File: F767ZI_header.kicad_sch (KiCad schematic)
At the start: 21 parts, among them J2 CAN1, J3 CAN2, J4 UART, J5 PowerBoard, J6 EMERSW_CON, J7 I2C1_default, J9 RESET_SW, SW1 SW_Push, U1 MCP2562-E-P, U2 MCP2562-E-P

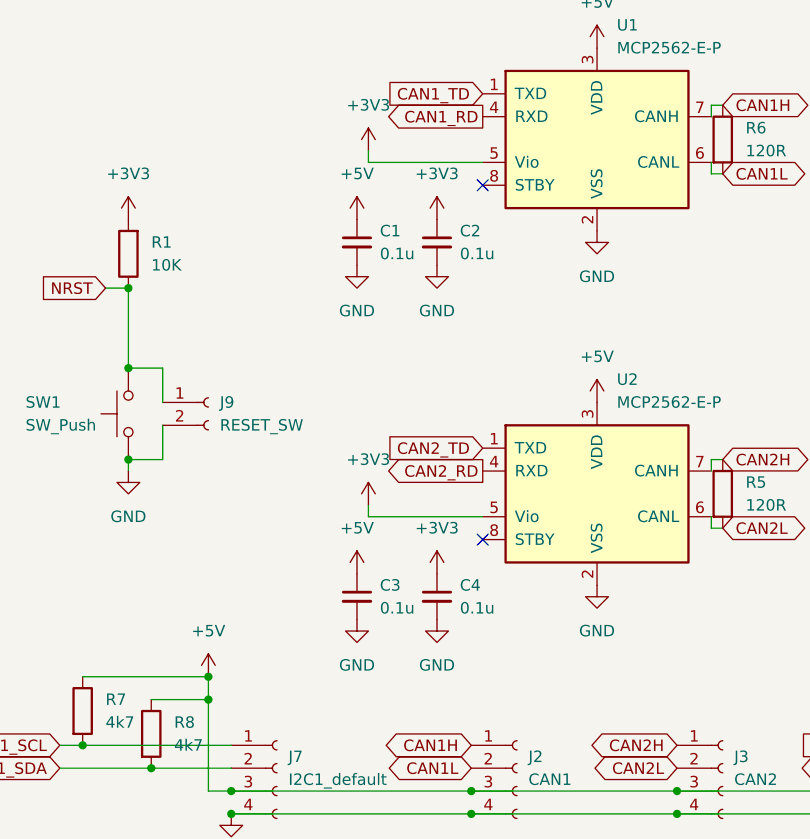
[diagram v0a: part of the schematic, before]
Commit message: SCH: トランシーバのSTBYをGNDに接続
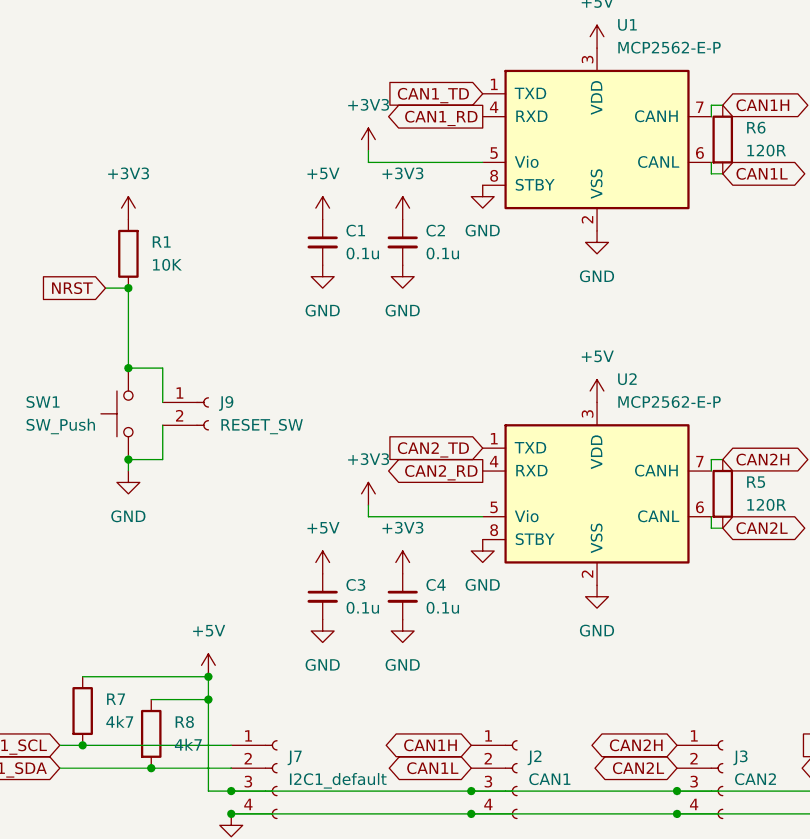
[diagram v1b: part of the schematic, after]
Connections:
- net GND: now also U1.8 (STBY), U2.8 (STBY)
- no-connect marks 79 -> 77
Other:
- moved on the sheet: C1, C2, C3, C4
